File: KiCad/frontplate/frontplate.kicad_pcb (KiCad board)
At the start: 2 copper layers, 88 x 79.8 mm, 5 parts

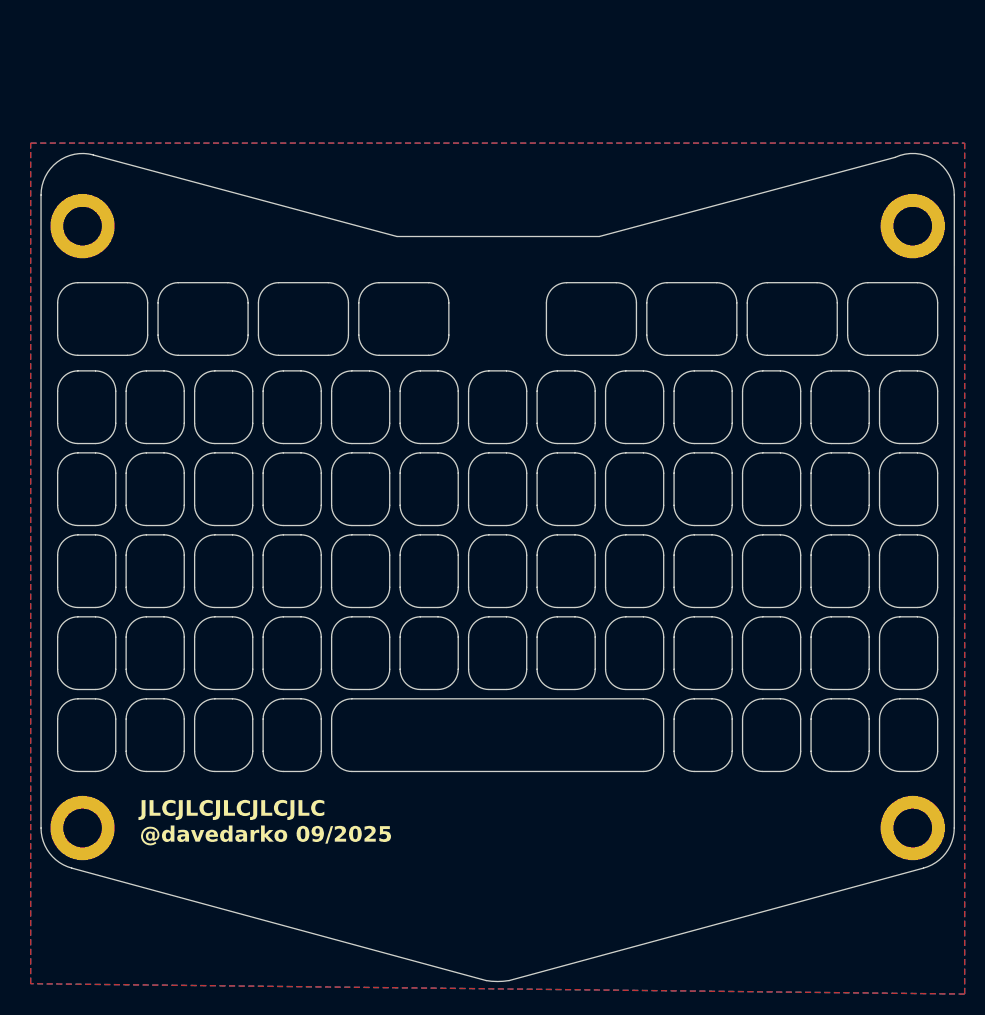
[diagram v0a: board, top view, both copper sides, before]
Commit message: Modify for EMF camp - Change shape - Move standoffs to bottom PCB - Add RGB LEDs and power conversion for them - Add art - Generate and add 3D models
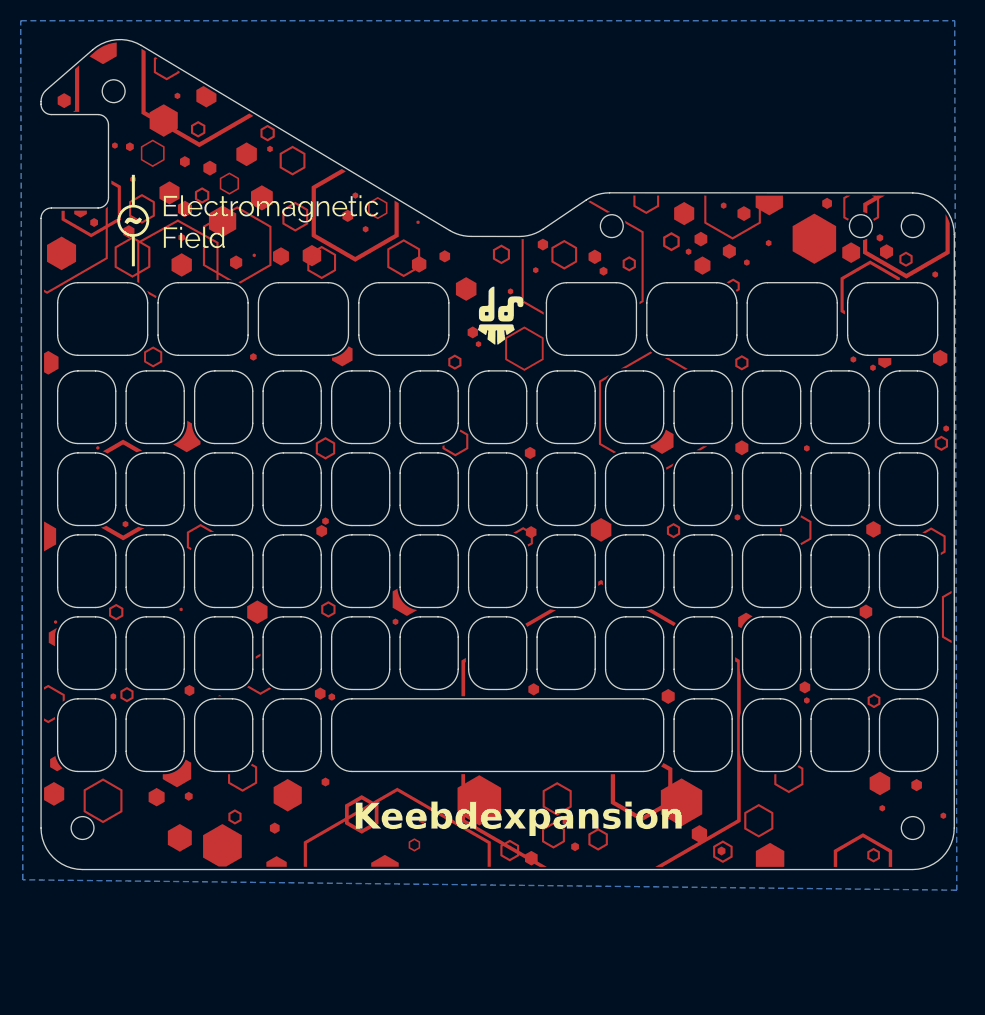
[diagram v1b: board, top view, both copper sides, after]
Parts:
- added H5: MountingHole, MountingHole:MountingHole_2.2mm_M2, F.Cu at (11.0, -29.0)
- added H6: MountingHole, MountingHole:MountingHole_2.2mm_M2, F.Cu at (40.0, -29.0)
- H1, H2: footprint frontplate:SMTSO2020CTJ -> MountingHole:MountingHole_2.2mm_M2; moved to B.Cu
- H3, H4: footprint frontplate:SMTSO2020CTJ -> MountingHole:MountingHole_2.2mm_M2
- moved H4 13.3 mm to (-37.0, -42.0)
- moved H3 5.00 mm to (35.0, -29.0)
- turned H1 to 180 degrees
- turned H2 to 180 degrees
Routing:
- added copper zone on B.Cu, net (none)
- removed copper zone on B.Cu, net GND
- removed copper zone on F.Cu, net GND
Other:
- board size 88 x 79.8 mm -> 88 x 80 mm
- board text added: "Artwork by Morag Hickman"
- board text added: "Keebdexpansion"
- board text added: "Keebdexpansion v1.0.3 2026"
- board text added: "PCB sponsored by:"
- board text added: "Updated by Kliment 05/2026"
- board text removed: "JLCJLCJLCJLCJLC"
